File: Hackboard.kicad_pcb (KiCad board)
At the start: 4 copper layers, 101 x 53.3 mm, 65 parts, among them J1 Conn_01x24, J2 Micro_SD_Card, J3 Conn_01x10, J4 Conn_01x08, J5 Conn_02x02_Counter_Clockwise, J6 USB_C_Receptacle_USB2.0_16P, J7 Barrel_Jack_Switch, J8 Conn_01x20, Q1 PSMN041, Q2 PSMN041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

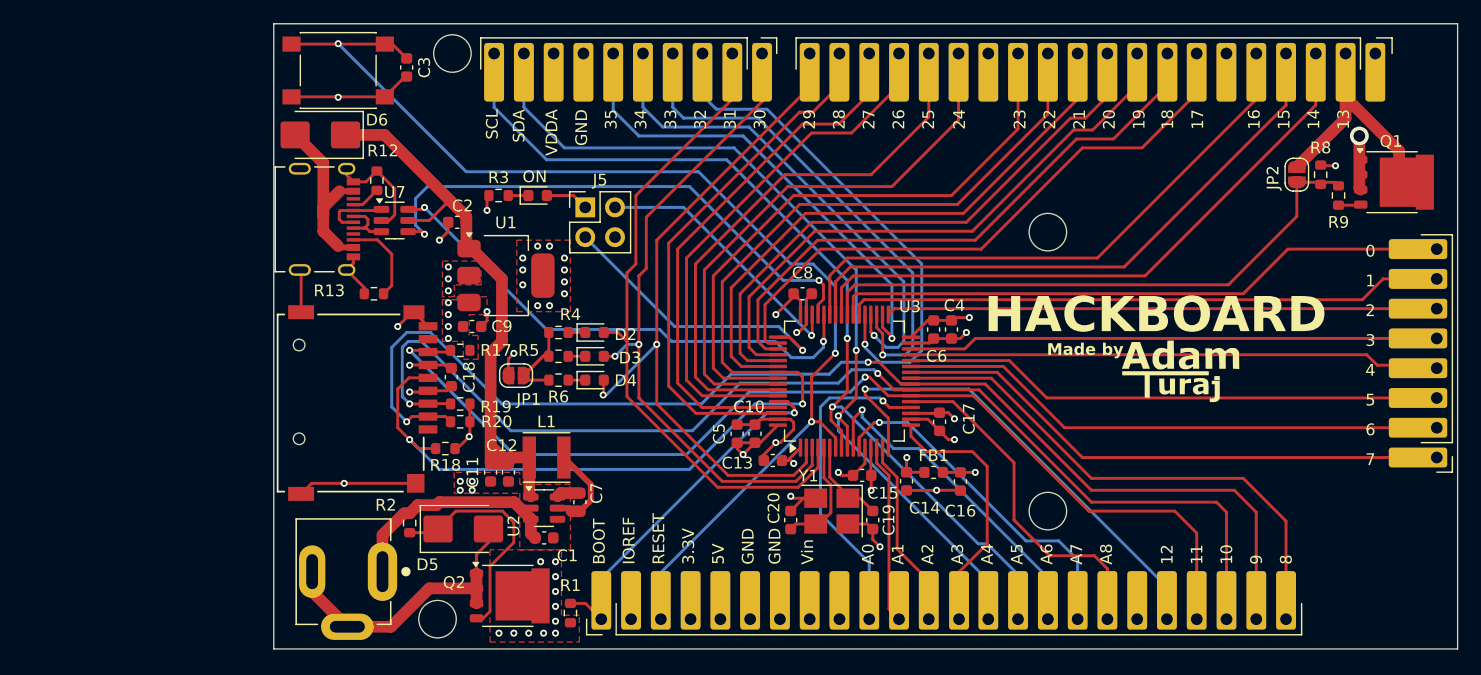
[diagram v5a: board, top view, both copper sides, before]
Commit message: Fix footprint for HSE, add logo and updated schematic
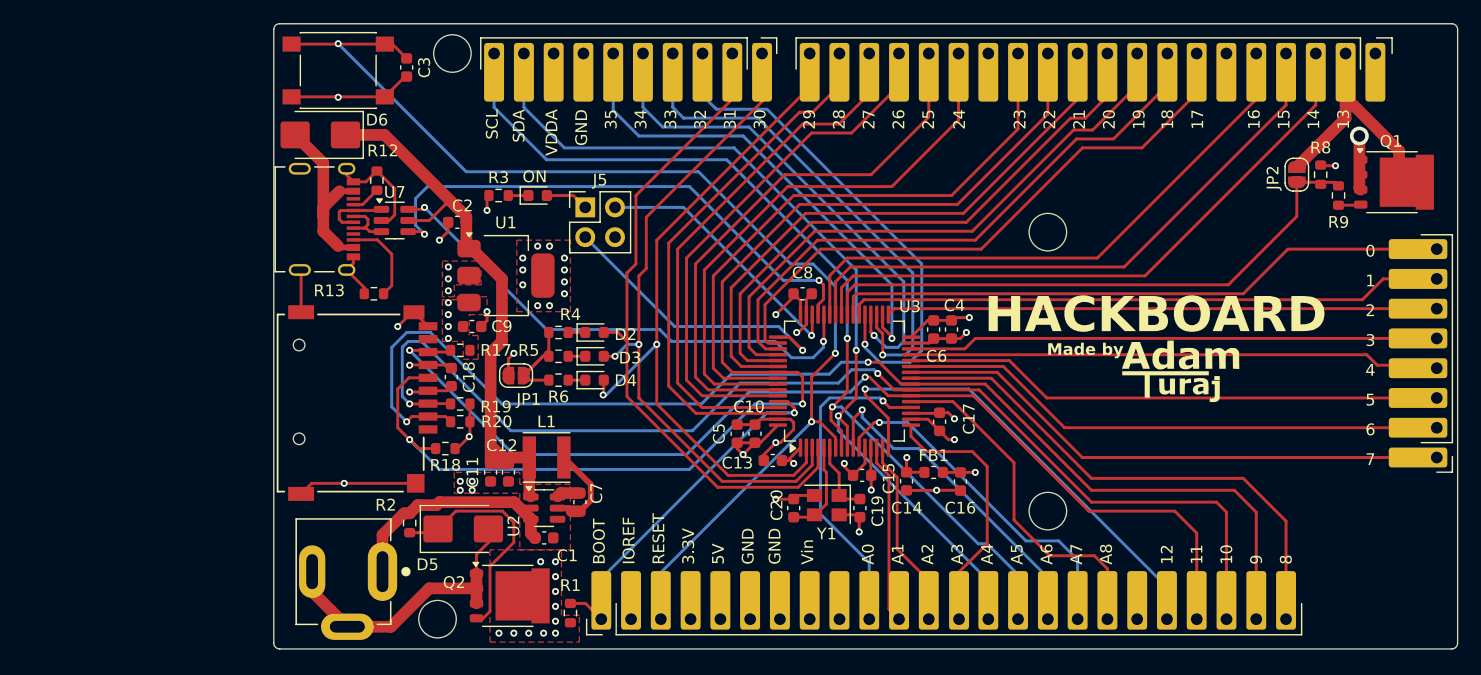
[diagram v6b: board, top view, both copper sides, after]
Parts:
- Y1: footprint Oscillator:Oscillator_SMD_Abracon_ASE-4Pin_3.2x2.5mm_HandSoldering -> Oscillator:Oscillator_SMD_Abracon_ASE-4Pin_3.2x2.5mm
- moved C19 1.49 mm to (151.7, 116.8)
- moved C20 1.05 mm to (146.1, 116.8)
- moved Y1 0.66 mm to (148.9, 116.6)
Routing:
- net VDDA: track 59.1 -> 61.6 mm
- net GND: track 94.1 -> 92.2 mm
- net Net-(U3-PH0): track 9.80 -> 8.16 mm
- net Net-(U3-PH1): track 7.53 -> 6.31 mm
- net VCC: track 130.6 -> 131.3 mm
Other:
- outline, holes or cut-outs redrawn

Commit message: Make some changes to the README
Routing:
- net PWM_12: track 41.3 -> 42.1 mm
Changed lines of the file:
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@@
 	)
 	(segment
-		(start 177.894001 123.5839)
+		(start 152.146 106.68)
+		(end 162.306 106.68)
+		(width 0.25)
+		(layer "B.Cu")
+		(net 82)
+	)
+	(segment
+		(start 177.894001 122.268001)
 		(end 177.894001 126.314)
 		(width 0.25)
@@
 	)
 	(segment
-		(start 160.990101 106.68)
-		(end 177.894001 123.5839)
+		(start 162.306 106.68)
+		(end 177.894001 122.268001)
 		(width 0.25)
 		(layer "B.Cu")
-		(net 82)
-	)
-	(segment
-		(start 152.146 106.68)
-		(end 160.990101 106.68)
-		(width 0.25)
-		(layer "B.Cu")

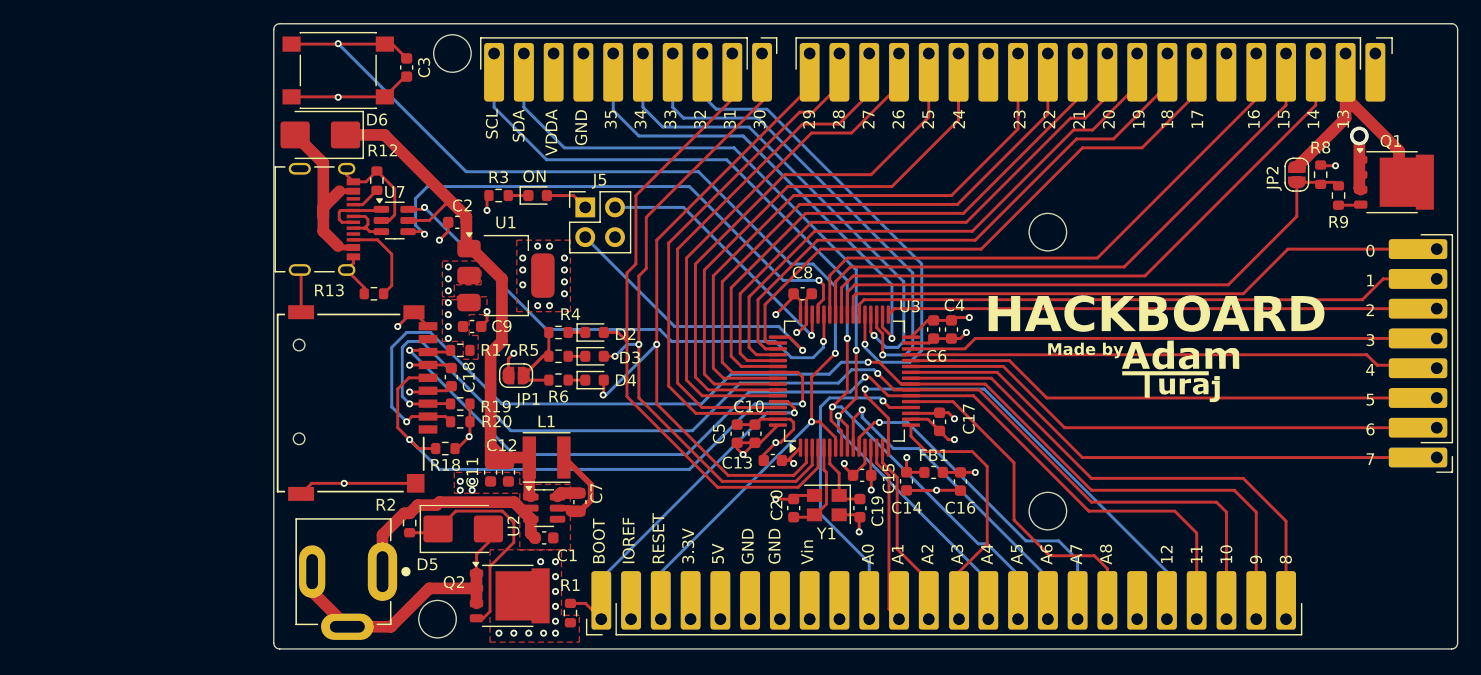
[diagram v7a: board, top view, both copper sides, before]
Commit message: Rotate MCU and retrace
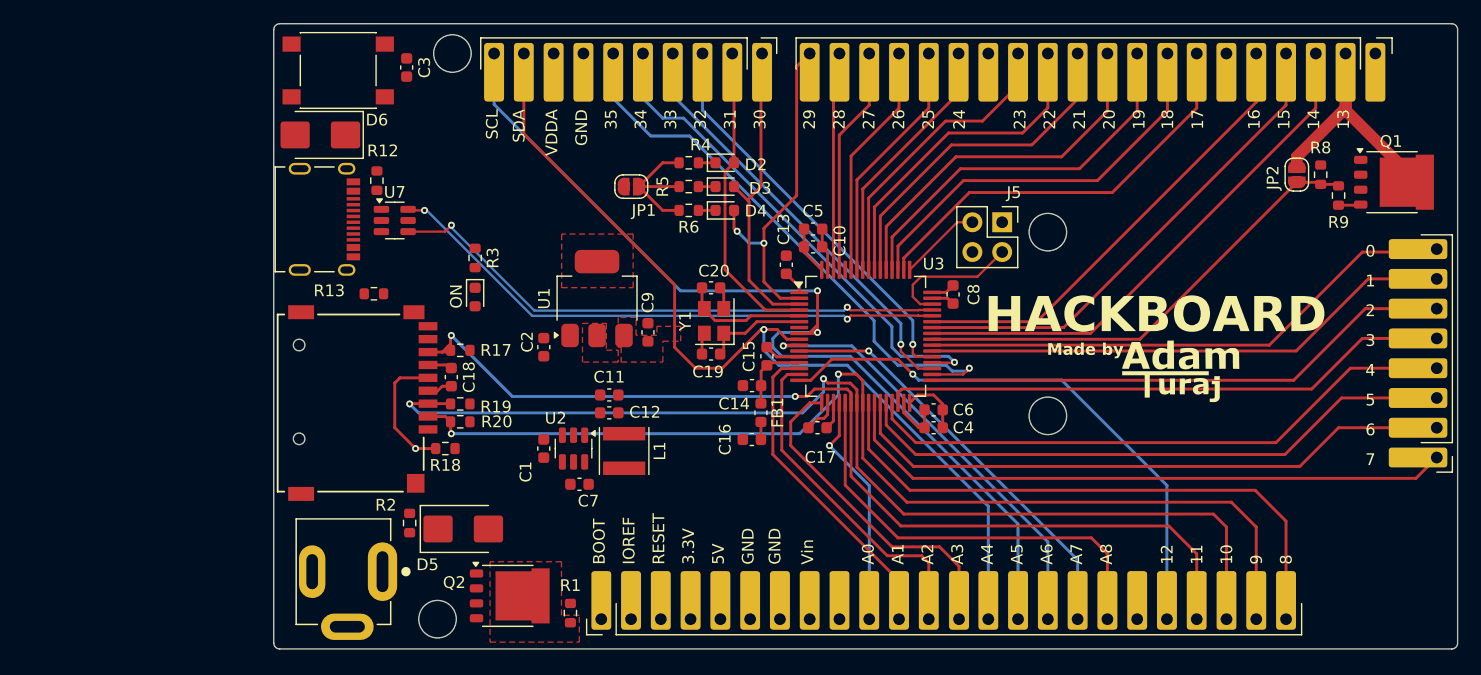
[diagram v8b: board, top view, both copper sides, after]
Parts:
- moved J5 35.6 mm to (163.8, 92.5), turned to -90 degrees
- moved C20 20.1 mm to (139.0, 98.0), turned to 0 degrees
- moved JP1 18.9 mm to (132.2, 89.4)
- moved C5 18.6 mm to (147.7, 93.0), turned to 0 degrees
- moved Y1 18.4 mm to (139.3, 100.9), turned to 90 degrees
- moved C19 18.3 mm to (139.0, 103.7), turned to 180 degrees
- moved R6 18.3 mm to (137.1, 91.4)
- moved D4 18.3 mm to (140.2, 91.4)
- moved R4 18.3 mm to (137.1, 87.4)
- moved R5 18.3 mm to (137.1, 89.4)
- moved D2 18.3 mm to (140.2, 87.4)
- moved D3 18.3 mm to (140.2, 89.4)
- moved C16 18.1 mm to (142.5, 111.0), turned to 0 degrees
- moved C13 16.7 mm to (145.4, 96.1), turned to 90 degrees
- moved C10 16.7 mm to (147.7, 94.6), turned to 0 degrees
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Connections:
- net USB_DM renamed USB_DN
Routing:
- net RESET: track 99.4 -> 0.00 mm, vias 3 -> 0
- net GND: track 92.2 -> 22.4 mm, vias 46 -> 0
- net SD_SCK_22: track 102.6 -> 39.5 mm, vias 2 -> 1
- net +5V: track 49.1 -> 0.00 mm
- net BOOT: track 31.0 -> 0.00 mm, vias 1 -> 0
- net GPIO_29: track 60.0 -> 29.3 mm
- net GPIO_31: track 57.2 -> 26.6 mm
- net GPIO_30: track 57.0 -> 26.7 mm, vias 2 -> 0
- net CAN_TX_28: track 45.4 -> 18.7 mm
- net PWM_25: track 47.7 -> 21.0 mm
- net CAN_RX_27: track 46.1 -> 19.5 mm
- net Net-(D5-A): track 26.5 -> 0.00 mm
- net PWM_24: track 48.2 -> 21.8 mm
- net PWM_23: track 51.4 -> 25.6 mm
- net PWM_26: track 45.7 -> 20.1 mm
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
